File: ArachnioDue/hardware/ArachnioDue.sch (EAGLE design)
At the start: 60 parts, among them J5 HEAD17-NOSS, J6 HEAD17-NOSS, Q1 8MHz, T1 FDN340P/PMV48XP, U1 ATMEGA32U4-XUMU, U2 AP2111HA-3.3, U3 ZLDO1117-5.0, U5 ESP8266EX, U6 SPI_FLASH, Y1 26 MHz/10 pF

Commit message: -- Captured schematic for SAM3S*A version
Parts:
- removed C15: 10u/6.3V, resistor:C-EUC0603
- removed GPIO0, GPIO2, MTDO, OTA: JUMPER-PAD-2-NOYES_SILK, SparkFun-Passives:JUMPER-PAD-2-NOYES_SILK
- removed L2: MH2029-300Y, wuerth-elektronik:WE-CBF_0805
- removed R12: 0R, resistor:R-EU_R0603
- removed R4: 10K, resistor:R-EU_R0603
- removed R6: 1K, resistor:R-EU_R0603
- removed T1: FDN340P/PMV48XP, zetex:PMOSSOT23
- removed TX: YLW, led:LEDCHIP-LED0603
- removed U3: ZLDO1117-5.0, logos-power:ZLDO1117-5.0
- added C12, C13, C2, C20, C21, C22, C27, C28, C29: 100n, resistor:C-EUC0402
- added C14: 2u2, resistor:C-EUC0603
- added C23, C24, C25, C26: 4u7, resistor:C-EUC0603
- added D1, D2: CGRM4001-G, diode:CGRM4001-G
- added ERASE: SPST_TACT-KMR2, adafruit:SPST_TACT-KMR2
- added L1: 10u/100mA, wuerth-elektronik:WE-CBF_0805
- added LOAD/OTA: JUMPER-PAD-3-NOYES_SILK, SparkFun-Passives:JUMPER-PAD-3-NOYES_SILK
- added RST: JUMPER-PAD-2-NC_BY_TRACE, SparkFun-Passives:JUMPER-PAD-2-NC_BY_TRACE
- added Y2: (no value), SparkFun-FreqCtrl:CRYSTALEPSONMC146
- C10, C6: value 100n -> 4u7; PARTNO CC0603ZRY5V9BB104 -> CL21F475ZPFNNNE; VOLTAGE (none) -> 10V
- C11: device resistor:C-EUC0603 -> resistor:C-EUC0402; PARTNO CC0603ZRY5V9BB104 -> CC0402KRX7R7BB104; VOLTAGE (none) -> 16V
- C16, C17, C18, C19: device resistor:C-EUC0603 -> resistor:C-EUC0402
- C5: value 1uF -> 100n; device resistor:C-EUC0603 -> resistor:C-EUC0402; PARTNO C0603C105K3PACTU -> CC0402KRX7R7BB104; VOLTAGE (none) -> 16V
- C7: value 1uF -> 4u7; PARTNO C0603C105K3PACTU -> CL21F475ZPFNNNE; VOLTAGE (none) -> 10V
- CN1: device adafruit:USBMINIB -> SparkFun-Connectors:USB-AB
- Q1: value 8MHz -> 12MHz; PARTNO PRQC8.00CR1010V00L -> (none)
- R1, R10, R11, R13, R14, R2, R3, R5, R7, R8, R9: device resistor:R-EU_R0603 -> resistor:R-EU_R0402
- RN1: value 22R -> 27R; PARTNO EXB-V4V220JV -> (none)
- U1: value ATMEGA32U4-XUMU -> SAM3SA-MU; device SmartPrj:ATMEGA32U4-XUMU -> atmel-sam3s:SAM3SA-MU; PARTNO ATMEGA32U4-MU -> (none)
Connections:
- removed net +5V: C3.1, J6.6, R5.1, T1.S, U2.IN, U3.OUT, U3.OUT@1
- removed net AVCC: C7.1, L2.2, U1.AVCC1
- removed net CHIP_EN: J6.7, R11.2, U5.CHIP_EN
- removed net D4*: J5.9, U1.(ICP1/ADC8)PD4
- removed net D5*: J5.10, U1.(OC3A/#0C4A)PC6
- removed net D6*: J5.11, U1.(T0/OC4D/ADC10)PD7
- removed net D7: J5.12, U1.(INT6/AIN0)PE6
- removed net ESP_RST: J6.8, R12.2, R14.2, U5.XPD_DCDC
- removed net HWB: R4.1, U1.(#HWB)PE2
- removed net IO10*: J5.15, U1.(PCINT6/OC1B/OC4B/ADC13)PB6
- removed net IO11*: J5.16, U1.(PCINT7/OC0A/OC1C/#RTS)PB7
- removed net IO12*: J5.17, U1.(T1/#OC4D/ADC9)PD6
- removed net IO13: J6.17, R8.1, U1.(ICP3/CLK0/OC4A)PC7
- removed net IO8: J5.13, U1.(ADC11/PCINT4)PB4
- removed net IO9*: J5.14, U1.(PCINT5/OC1A/#OC4B/ADC12)PB5
- removed net N$4: R6.2, TX.A
- removed net RXLED/SS: J5.2, R7.1, U1.(SS/PCINT0)PB0
- removed net TXLED: R6.1, U1.(XCK1/#CTS)PD5
- removed net UCAP: C5.1, U1.UCAP
- new net D10: J5.15, U1G$5.PA15/PGMD3
- new net D11: J5.16, U1G$5.PA1/PGMEN1
- new net D12: J5.17, U1G$5.PA2/PGMEN2
- new net D13: J6.17, R8.1, U1G$5.PA0/PGMEN0
- new net D4: J5.9, U1G$4.PB2/AD6
- new net D5: J5.10, U1G$4.PB4/TDI
- new net D6: J5.11, U1G$4.PB3/AD7
- new net D8: J5.13
- new net D9: J5.14, U1G$5.PA11/PGMM3
- new net ERASE: ERASE.S, ERASE.S1, J6.7, R9.2, U1G$4.PB12/ERASE
- new net ESP_RX: TP2.TP, U1G$5.PA10/PGMM2, U5.U0RXD
- new net ESP_TX: TP1.TP, U1G$5.PA9/PGMM1, U5.U0TXD
- new net N$8: C3.1, C4.1, D1.C, D2.C, U2.IN
- new net RXTXLED/SS: J5.2, R7.1, U1G$6.PA16/PGMD4
- new net SWCLK/D8: U1G$4.PB7/TCK/SWCLK
- new net SWDIO/D7/CHIP_EN: J5.12, R11.2, U1G$4.PB6/TMS/SWDIO, U5.CHIP_EN
- new net SWO/ESP_RST: J6.8, R14.2, RST.2, U1G$4.PB5/TDO/TRACESWO, U5.XPD_DCDC
- new net VDDOUT: C13.1, C14.1, L1.1, U1G$2.VDDCORE@0, U1G$2.VDDCORE@1, U1G$2.VDDOUT
- new net VDDPLL: C2.1, C5.1, C6.1, L1.2, U1G$2.VDDPLL
- net 3V3: now also C20.1, C21.1, C22.1, C23.1, C24.1, C25.1, C26.1, C27.1, C28.1, C29.1, C7.1, ERASE.P, ERASE.P1, R10.2, R5.1, RX.A, U1G$2.VDDIN, U1G$2.VDDIO@0, U1G$2.VDDIO@1, U1G$2.VDDIO@2, U5.GPIO2; no longer C15.1, L2.1, U1.AVCC, U1.UVCC, U1.VCC, U1.VCC1
- net A0: now also U1G$6.PA17/PGMD5/AD0; no longer U1.(ADC7/TDI)PF7
- net A1: now also U1G$6.PA18/PGMD6/AD1; no longer U1.(ADC6/TDO)PF6
- net A2: now also U1G$6.PA19/PGMD7/AD2; no longer U1.(ADC5/TMS)PF5
- net A3: now also U1G$6.PA20/PGMD8/AD3; no longer U1.(ADC4/TCK)PF4
- net A4: now also U1G$4.PB0/AD4; no longer U1.(ADC1)PF1
- net A5: now also U1G$4.PB1/AD5; no longer U1.(ADC0)PF0
- net AREF: now also C12.2, U1G$2.ADVREF; no longer C6.1, U1.AREF
- net D0/RX: now also U1G$5.PA5/PGMRDY; no longer U1.(RXD1/AIN1/INT2)PD2, U5.U0TXD
- net D1/TX: now also U1G$5.PA6/PGMNOE; no longer U1.(TXD1/INT3)PD3, U5.U0RXD
- net D2/SDA: now also U1G$5.PA3; no longer GPIO2.2, U1.(SDA/INT1)PD1
- net D3/SCL: now also LOAD/OTA.3, U1G$5.PA4/PGMNCMD; no longer GPIO0.2, U1.(OC0B/SCL/INT0)PD0
- net GND: now also C12.1, C13.2, C14.2, C2.2, C20.2, C21.2, C22.2, C23.2, C24.2, C25.2, C26.2, C27.2, C28.2, C29.2, U1G$1.TST, U1G$3.GND@0, U1G$3.GND@1, U5.MTDO; no longer C15.2, R10.1, R4.2, RX.C, TX.C, U1.GND, U1.GND1, U1.GND2, U1.GND3, U1.PAD, U1.UGND, U3.GND
- net MISO: now also U1G$5.PA12/PGMD0; no longer U1.(PD0/MISO/PCINT3)PB3
- net MOSI: now also U1G$5.PA13/PGMD1; no longer MTDO.2, U1.(PDI/MOSI/PCINT2)PB2
- net N$1: now also U1G$5.PA8/XOUT32/PGMM0, Y2.1; no longer MTDO.1, R10.2, TP1.TP, U5.MTDO
- net N$2: now also RX.C; no longer RX.A
- net N$33: now also RST.1; no longer R12.1
- net N$5: now also U1G$5.PA7/XIN32/PGMNVALID, Y2.2; no longer GPIO2.1, TP2.TP, U5.GPIO2
- net N$6: now also LOAD/OTA.2, R10.1; no longer GPIO0.1, OTA.1
- net RD+: now also U1G$4.PB11/DDP; no longer U1.D+
- net RD-: now also U1G$4.PB10/DDM; no longer U1.D-
- net RESET: now also LOAD/OTA.1, U1G$1.NRST; no longer OTA.2, U1.RESET
- net SCK: now also U1G$5.PA14/PGMD2; no longer U1.(SCLK/PCINT1)PB1
- net VIN: now also D2.A; no longer C4.1, R9.2, T1.G, U3.IN
- net VUSB: now also D1.A, J6.6; no longer T1.D, U1.VBUS
- net XTAL1: now also U1G$4.PB9/XIN/PGMCK; no longer U1.XTAL1
- net XTAL2: now also U1G$4.PB8/XOUT; no longer U1.XTAL2
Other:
- note removed: "#PWM 10bit"
- note removed: "#PWM 16bit"
- note removed: "#PWM 8/16bit"
- note removed: "#PWM 8bit"
- note removed: "#PWM Hi-Speed"
- note removed: "+5V REG"
- note removed: "+5V SELECTOR (USB)"
- moved on the sheet: C1, C18, C3, C4, L, Q1, R10, R7, R8, RN1A, RN1B, RX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

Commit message: ﻿First test boards of this design # Please enter the commit message for your changes. Lines starting # with '#' will be ignored, and an empty message aborts the commit. # On branch master # Your branch is ahead of 'origin/master' by 1 commit. #   (use "git push" to publish your local commits) # # Changes to be committed: #	new file:   ArachnioDue/hardware/ArachnioDue.G15L #	new file:   ArachnioDue/hardware/ArachnioDue.G2L #	new file:   ArachnioDue/hardware/ArachnioDue.GBL #	new file:   ArachnioDue/hardware/ArachnioDue.GBO #	new file:   ArachnioDue/hardware/ArachnioDue.GBS #	new file:   ArachnioDue/hardware/ArachnioDue.GDM #	new file:   ArachnioDue/hardware/ArachnioDue.GML #	new file:   ArachnioDue/hardware/ArachnioDue.GTL #	new file:   ArachnioDue/hardware/ArachnioDue.GTO #	new file:   ArachnioDue/hardware/ArachnioDue.GTS #	new file:   ArachnioDue/hardware/ArachnioDue.TXT #	modified:   ArachnioDue/hardware/ArachnioDue.brd #	new file:   ArachnioDue/hardware/ArachnioDue.gcb #	new file:   ArachnioDue/hardware/ArachnioDue.gct #	new file:   ArachnioDue/hardware/ArachnioDue.oln #	modified:   ArachnioDue/hardware/ArachnioDue.sch #	new file:   ArachnioDue/hardware/ArachnioDue.zip #
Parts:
- removed TP1, TP2: PTR1TP15SQ, testpad:PTR1TP15SQ
- added C15: 100n, resistor:C-EUC0402
- D1, D2: value CGRM4001-G -> (none); device diode:CGRM4001-G -> SparkFun-DiscreteSemi:DIODESOD123
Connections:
- removed net D8: J5.13
- removed net ESP_RX: TP2.TP, U1G$5.PA10/PGMM2, U5.U0RXD
- removed net ESP_TX: TP1.TP, U1G$5.PA9/PGMM1, U5.U0TXD
- removed net N$8: C3.1, C4.1, D1.C, D2.C, U2.IN
- removed net SWDIO/D7/CHIP_EN: J5.12, R11.2, U1G$4.PB6/TMS/SWDIO, U5.CHIP_EN
- new net CHIP_EN: R11.2, U1G$5.PA15/PGMD3, U5.CHIP_EN
- new net SWDIO/D7: J5.12, U1G$4.PB6/TMS/SWDIO
- new net VCC: C3.1, C4.1, D1.C, D2.C, J6.6, U2.IN
- net D0/RX: now also U1G$5.PA9/PGMM1, U5.U0TXD; no longer U1G$5.PA5/PGMRDY
- net D1/TX: now also U1G$5.PA10/PGMM2, U5.U0RXD; no longer U1G$5.PA6/PGMNOE
- net D10: now also U1G$5.PA2/PGMEN2; no longer U1G$5.PA15/PGMD3
- net D12: now also U1G$5.PA11/PGMM3; no longer U1G$5.PA2/PGMEN2
- net D4: now also U1G$4.PB3/AD7; no longer U1G$4.PB2/AD6
- net D6: now also U1G$4.PB2/AD6; no longer U1G$4.PB3/AD7
- net D9: now also U1G$5.PA5/PGMRDY; no longer U1G$5.PA11/PGMM3
- net GND: now also C15.2
- net SWCLK/D8: now also J5.13
- net VDDOUT: now also C15.1
- net VUSB: no longer J6.6
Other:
- moved on the sheet: C12, C14, C2, C20, C21, C22, C23, C24, C5, C6, L1, U1G$2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

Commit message: Pre-prototype check-in
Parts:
- C1: PARTNO C0603C105K3PACTU -> generic MLCC:1u/25V/0603
- C10, C23, C24, C25, C26, C6, C7: PARTNO CL21F475ZPFNNNE -> generic MLCC:4u7/10V/0603
- C11, C13, C15, C20, C21, C22, C27, C28, C29, C5: PARTNO CC0402KRX7R7BB104 -> generic MLCC:100n/16V/0402
- C12, C2: PARTNO (none) -> generic MLCC:100n/16V/0402
- C14: PARTNO JMK107BJ225KAHT -> generic MLCC:2u2/6V3/0603
- C16, C17: PARTNO C0603C100K5GACTU -> (none)
- C18: PARTNO 251R14S5R6CV4T -> (none)
- C19: PARTNO CC0603ZRY5V9BB104 -> generic MLCC:100n/16V/0402
- C3, C4, C8: PARTNO CL10A475KA8NQNC -> generic MLCC:4u7/25V/0603
- C9: PARTNO CC0603ZRY5V9BB104 -> generic MLCC:100n/50V/0603
- CN1: PARTNO USB-M26FTR -> 10104111-0001LF
- D1, D2: PARTNO (none) -> CDBW140-G
- J5, J6, LOAD/OTA: BOM (none) -> EXCLUDE
- Q1: PARTNO (none) -> PRQC12.00CR1010V00L
- R1, R10, R11, R14, R2, R9: PARTNO RNCP0603FTD10K0 -> generic resistor:10K/0402
- R13: PARTNO MCR03ERTJ201 -> generic resistor:200R/0402
- R3: PARTNO RMCF0603FT12K0 -> generic resistor:12K/0402
- R5, R7, R8: PARTNO RMCF0603FT1K00 -> generic resistor:1K/0402
- RN1: PARTNO (none) -> EXB-V4V270JV
- U1: PARTNO (none) -> ATSAM4S2AA-MU
- Y2: PARTNO (none) -> MC-146 32.768KA-AC3
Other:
- moved on the sheet: U$11

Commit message: first module version, ready for mfg
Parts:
- removed C16, C17: 10 pF, resistor:C-EUC0402
- removed C18: 5p6, resistor:C-EUC0402
- removed C19, C27, C28, C29: 100n, resistor:C-EUC0402
- removed C25, C26: 4u7, resistor:C-EUC0603
- removed LOAD/OTA: JUMPER-PAD-3-NOYES_SILK, SparkFun-Passives:JUMPER-PAD-3-NOYES_SILK
- removed R10, R11, R14: 10K, resistor:R-EU_R0402
- removed R13: 200R, resistor:R-EU_R0402
- removed R3: 12K, resistor:R-EU_R0402
- removed RST: JUMPER-PAD-2-NC_BY_TRACE, SparkFun-Passives:JUMPER-PAD-2-NC_BY_TRACE
- removed TP3: PTR1TP15SQ, testpad:PTR1TP15SQ
- removed U$11: ANTENNA_1RIGHT, ant-planar-1:ANTENNA_1RIGHT
- removed U5: ESP8266EX, ESP8266:ESP8266EX
- removed U6: SPI_FLASH, ESP8266:SPI_FLASH
- removed Y1: 26 MHz/10 pF, SmartPrj:CRYSTAL-3.2-2.5
- added ERASE_JMP, RST_JMP: JUMPER-PAD-2-NOYES_SILK, SparkFun-Passives:JUMPER-PAD-2-NOYES_SILK
- added ESP1: ESP-12, esp8266-parts:ESP-12
- J5: value HEAD17-NOSS -> (none); device SmartPrj:HEAD17-NOSS -> logos-headers:PINHD-1X17_2.54-SMD-UNIVERSAL
- J6: device SmartPrj:HEAD17-NOSS-1 -> logos-headers:PINHD-1X17_2.54-SMD-UNIVERSAL
- U1: value SAM3SA-MU -> SAM3SB-AU; device atmel-sam3s:SAM3SA-MU -> atmel-sam3s:SAM3SB-AU
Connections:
- removed net N$27: C17.1, U5.XTAL_IN, Y1.C1
- removed net N$28: C16.1, U5.XTAL_OUT, Y1.C2
- removed net N$31: C18.1, U$11.RF
- removed net N$32: R3.1, U5.RES12K
- removed net N$33: RST.1, U5.EXT_RSTB
- removed net N$34: R13.2, U5.SD_CLK
- removed net N$35: R13.1, U6.CLK
- removed net N$36: U5.SD_CMD, U6./CS
- removed net N$37: U5.SD_DATA_2, U6./HOLD
- removed net N$38: U5.SD_DATA_3, U6./WP
- removed net N$39: U5.SD_DATA_1, U6.DIO
- removed net N$40: U5.SD_DATA_0, U6.D0
- removed net N$45: C18.2, U5.LNA
- removed net N$6: LOAD/OTA.2, R10.1, TP3.TP, U5.GPIO0
- removed net SWO/ESP_RST: J6.8, R14.2, RST.2, U1G$4.PB5/TDO/TRACESWO, U5.XPD_DCDC
- new net ESP_CS: ESP1.CS, U1G$6.PA23/PGMD11
- new net ESP_INT: ESP1.INT, U1G$6.PA24/PGMD12
- new net ESP_LOAD: ESP1.GPIO0
- new net ESP_RESET: ESP1.REST
- new net ESP_RX: ESP1.TXD, U1G$6.PA21/PGMD9/AD8
- new net ESP_TX: ESP1.RXD, U1G$6.PA22/PGMD10/AD9
- new net N$4: ESP1.GPIO13, RST_JMP.2
- new net N$8: ERASE_JMP.1, ESP1.GPIO12
- new net SWO: J6.8, U1G$4.PB5/TDO/TRACESWO
- net 3V3: now also ESP1.VCC; no longer C19.1, C25.1, C26.1, C27.1, C28.1, C29.1, R10.2, R11.1, R14.1, U5.GPIO2, U5.VDD1@2, U5.VDD3P3@1, U5.VDD3P3@2, U5.VDDA@1, U5.VDDD, U5.VDDPST@1, U5.VDDPST@2, U6.VCC
- net CHIP_EN: no longer R11.2, U5.CHIP_EN
- net D0/RX: no longer U5.U0TXD
- net D1/TX: no longer U5.U0RXD
- net D3/SCL: no longer LOAD/OTA.3
- net ERASE: now also ERASE_JMP.2
- net GND: now also ESP1.GND, U1G$7.GND@0, U1G$7.GND@1; no longer C16.2, C17.2, C19.2, C25.2, C26.2, C27.2, C28.2, C29.2, R3.2, U$11.GND, U5.GND, U5.MTDO, U6.GND, Y1.GND@1, Y1.GND@2
- net MISO: now also ESP1.MOSI
- net MOSI: now also ESP1.MISO
- net RESET: now also RST_JMP.1; no longer LOAD/OTA.1
- net SCK: now also ESP1.CLK

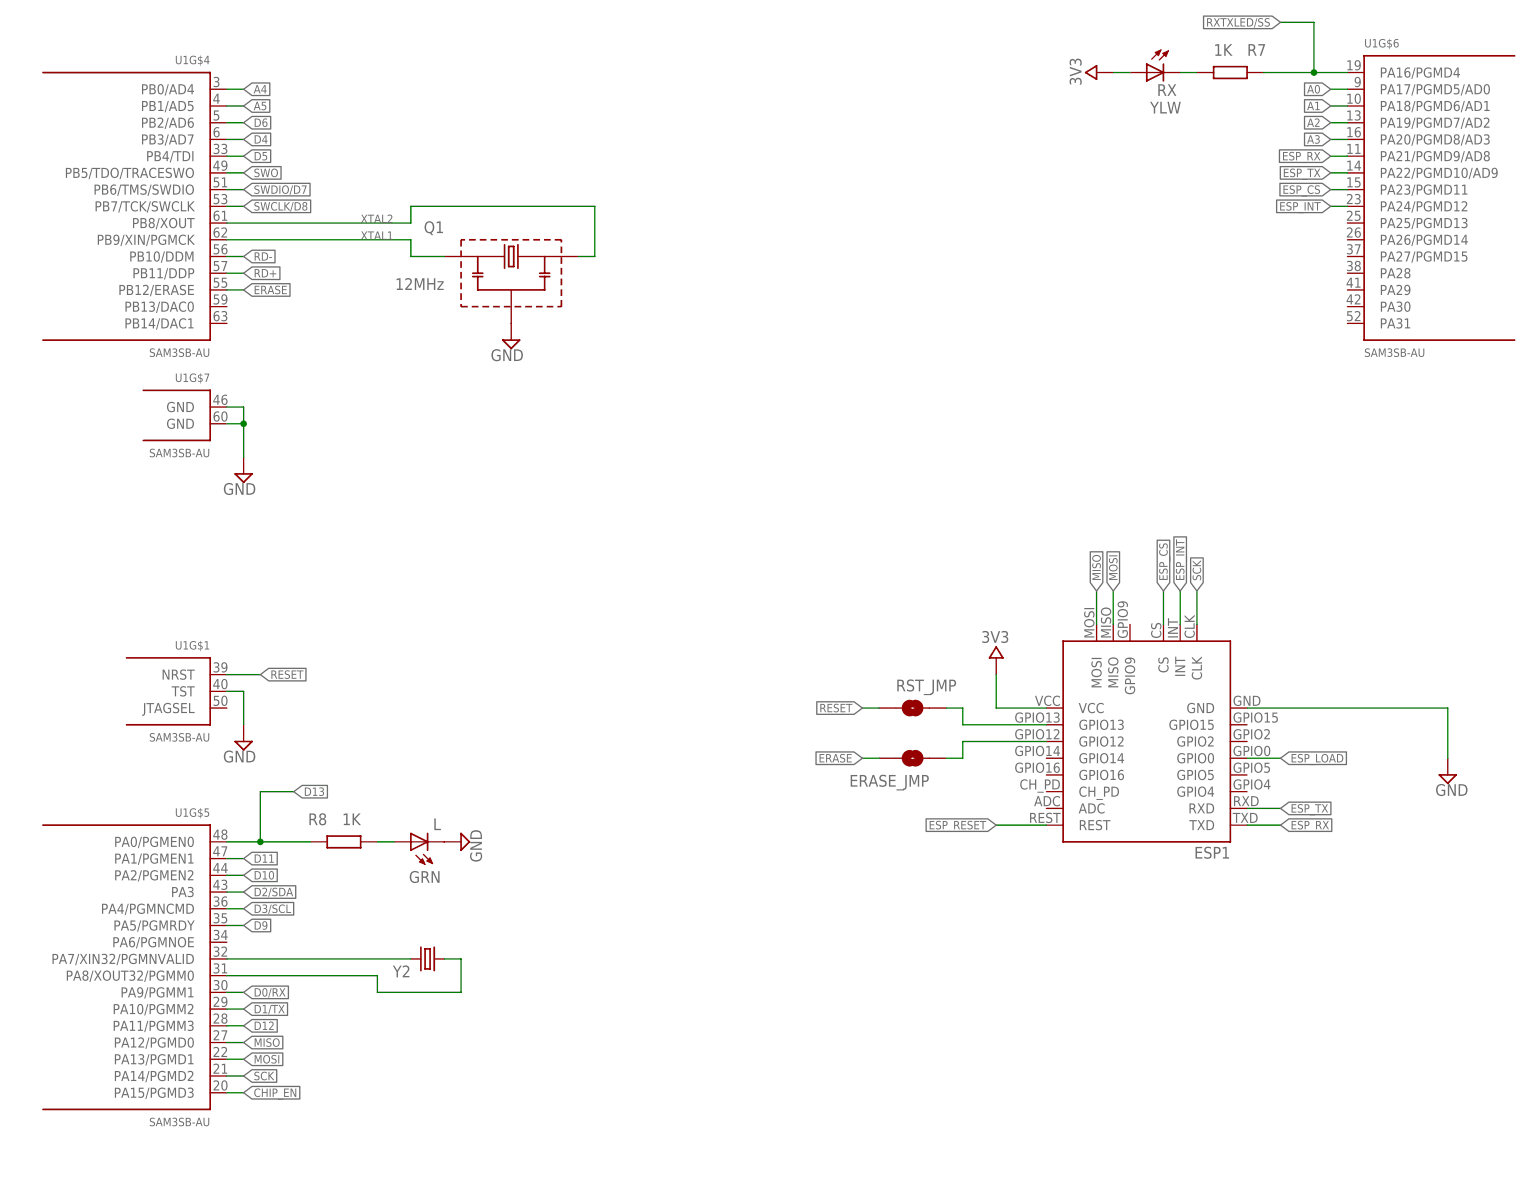
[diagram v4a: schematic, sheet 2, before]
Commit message: Re-arranged features, added test points
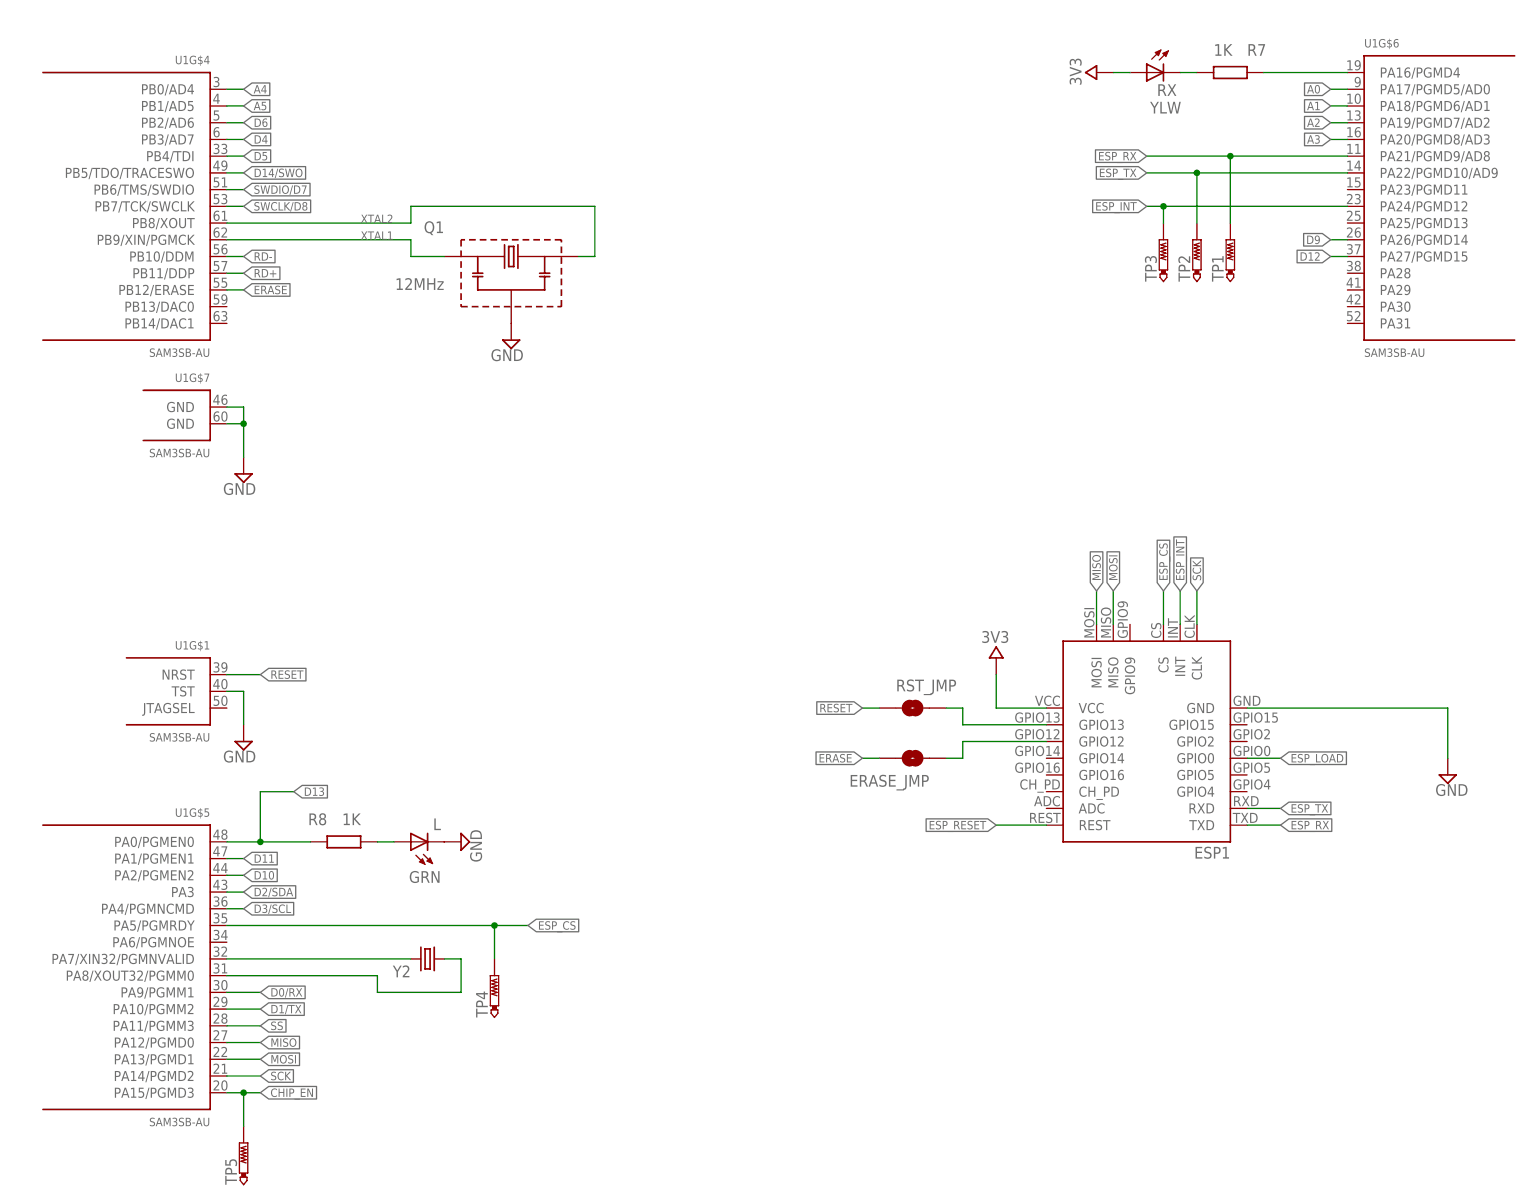
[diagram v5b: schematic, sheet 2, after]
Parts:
- added TP1, TP2, TP3, TP4, TP5: PTR1TP16R, testpad:PTR1TP16R
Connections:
- net SWO renamed D14/SWO
- removed net RXTXLED/SS: J5.2, R7.1, U1G$6.PA16/PGMD4
- new net RXTXLED: R7.1, U1G$6.PA16/PGMD4
- new net SS: J5.2, U1G$5.PA11/PGMM3
- net CHIP_EN: now also TP5.TP
- net D12: now also U1G$6.PA27/PGMD15; no longer U1G$5.PA11/PGMM3
- net D9: now also U1G$6.PA26/PGMD14; no longer U1G$5.PA5/PGMRDY
- net ESP_CS: now also TP4.TP, U1G$5.PA5/PGMRDY; no longer U1G$6.PA23/PGMD11
- net ESP_INT: now also TP3.TP
- net ESP_RESET: now also J6.5
- net ESP_RX: now also TP1.TP
- net ESP_TX: now also TP2.TP
- net RESET: no longer J6.5
